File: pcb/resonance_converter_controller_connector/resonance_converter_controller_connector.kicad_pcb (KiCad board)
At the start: 4 copper layers, 66.8 x 100 mm, 83 parts, among them J1 Conn_01x02, J10 Conn_01x04, J11 Conn_01x04, J12 Conn_01x02, J13 Conn_01x06, J14 Conn_02x05_Odd_Even, J15 Conn_01x02, J16 Conn_01x02, J17 Conn_01x02, J18 Conn_01x08, J19 Conn_01x02, J2 Conn_01x02, J20 Conn_01x02, J3 Conn_01x02, J4 Conn_01x04, J5 Conn_01x02, J6 FX18-120S-0.8SH, J7 Conn_01x04, J8 Conn_01x04, J9 Conn_01x04, Q1 Q_NMOS_GDS, Q2 Q_NMOS_GDS, Q3 Q_NMOS_GDS, Q4 Q_NMOS_GDS, Q5 Q_NPN_BEC, SW1 SW_DIP_x01, U1 PCF8574RGTR, U2 MIC29302AWU, U23 TPS2412D, U3 74LVC1G04, U4 TPS2412D, U5 TPS2412D, U6 TPS2412D, U7 TL431D, U8 AT24CS01-SSHM, U9 UA78M33QDCYRQ1

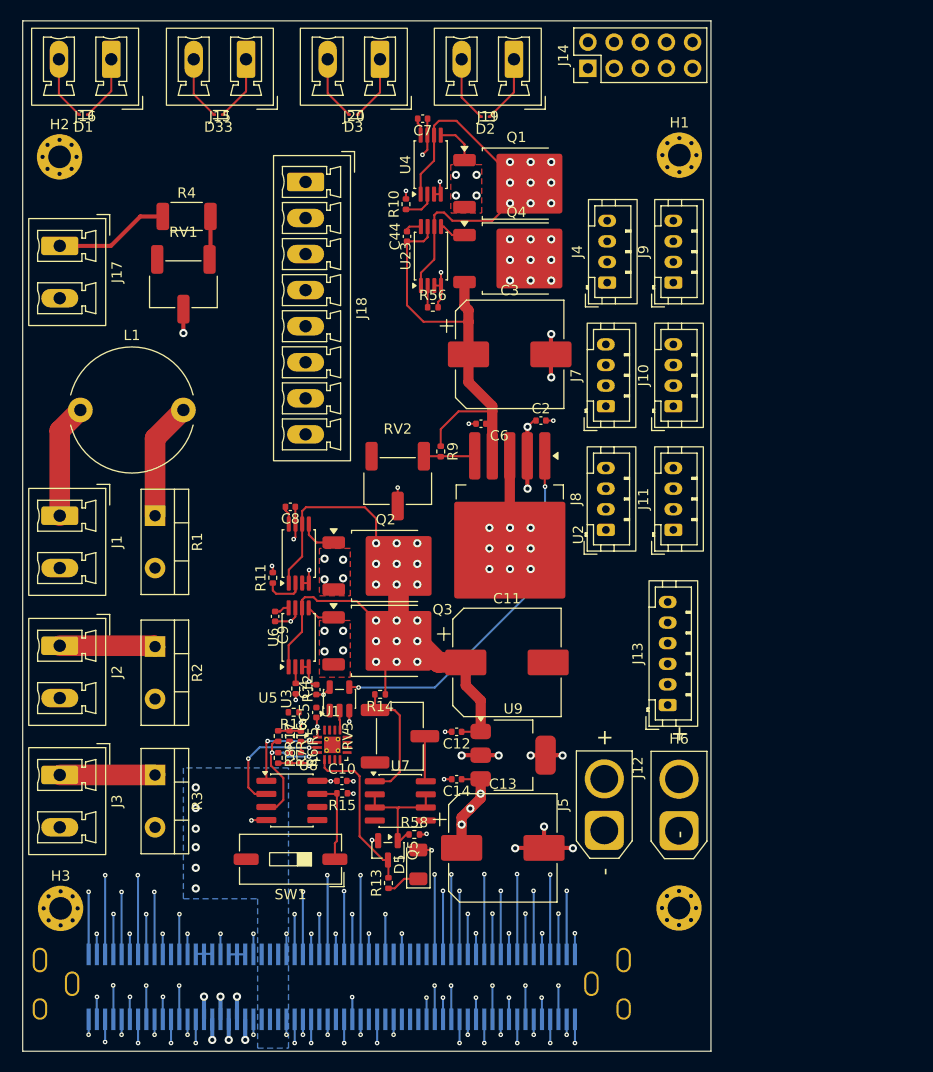
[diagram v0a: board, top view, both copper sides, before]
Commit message: connctor board routed
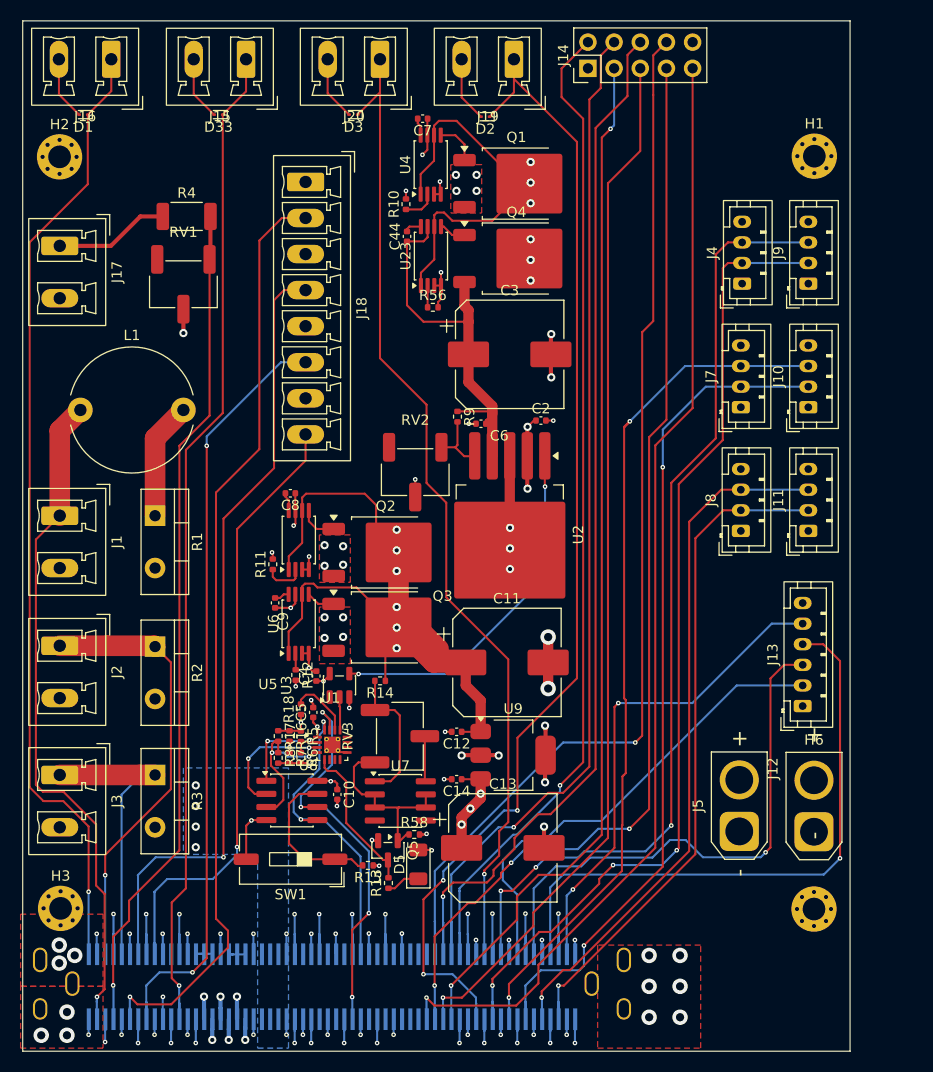
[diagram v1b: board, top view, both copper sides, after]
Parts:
- moved H1 13.1 mm to (192.0, 63.4)
- moved J5 13.1 mm to (184.8, 129.0)
- moved H6 13.1 mm to (192.0, 136.5)
- moved J12 13.1 mm to (192.0, 129.0)
- moved J13 13.1 mm to (190.9, 116.8)
- moved J10 13.1 mm to (191.4, 87.8)
- moved J11 13.1 mm to (191.4, 99.8)
- moved J4 13.1 mm to (185.0, 75.8)
- moved J7 13.1 mm to (184.9, 87.8)
- moved J8 13.1 mm to (184.9, 99.8)
- moved J9 13.1 mm to (191.4, 75.8)
- moved R15 7.43 mm to (148.7, 132.3)
- moved R9 3.75 mm to (157.4, 88.7)
- moved RV2 1.91 mm to (153.3, 94.1)
- moved C10 1.39 mm to (145.7, 125.4), turned to -90 degrees
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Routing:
- net GPIO3: track 2.05 -> 109.2 mm
- net GPIO2: track 3.23 -> 107.9 mm, vias 1 -> 3
- net AUX_PWM_CH1: track 8.60 -> 112.6 mm, vias 1 -> 3
- net GPIO1: track 2.05 -> 102.3 mm
- net GPIO4: track 7.72 -> 105.1 mm
- net GPIO0: track 3.23 -> 100.2 mm, vias 1 -> 2
- net GPIO5: track 6.11 -> 102.1 mm
- net OUT_SYNC_1-: track 3.22 -> 95.7 mm, vias 1 -> 3
- net GPIO6: track 7.71 -> 100.0 mm
- net GPIO7: track 6.11 -> 97.7 mm
- net ISENSE_1: track 2.14 -> 91.6 mm
- net DAC_OUT: track 9.53 -> 98.0 mm
- net OUT_SYNC_1+: track 6.11 -> 92.0 mm, vias 1 -> 3
- net OUT_SYNC_2+: track 2.05 -> 85.7 mm, vias 1 -> 2
- net AUX_PWM_CH2: track 14.0 -> 96.1 mm
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- added copper zone on In4.Cu, net GND
- removed copper zone on In2.Cu, net GND
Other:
- board size 66.8 x 100 mm -> 80.3 x 100 mm
- copper layers 4 -> 6

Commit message: Fix silkscreen
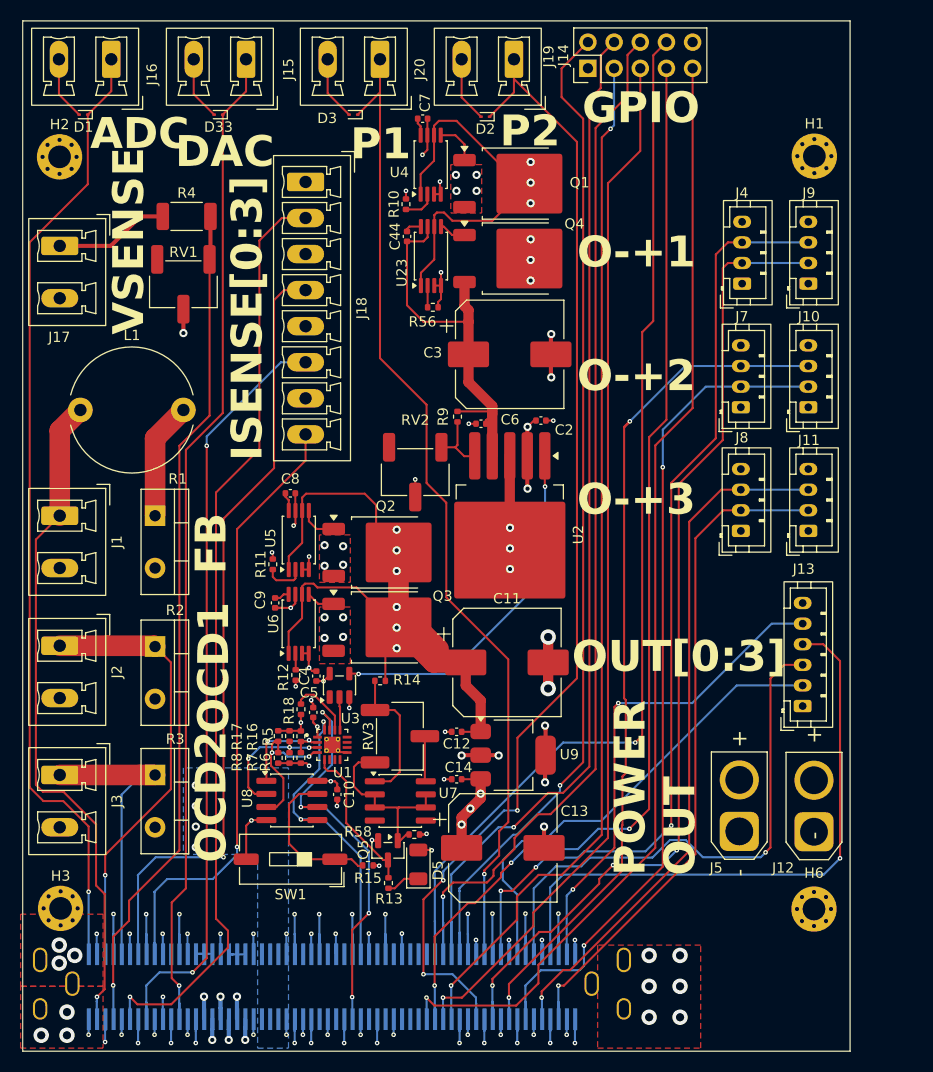
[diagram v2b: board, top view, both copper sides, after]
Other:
- board text added: "ADC"
- board text added: "DAC"
- board text added: "FB"
- board text added: "GPIO"
- board text added: "ISENSE[0:3]"
- board text added: "O-+1"
- board text added: "O-+2"
- board text added: "O-+3"
- board text added: "OCD1"
- board text added: "OCD2"
- board text added: "OUT[0:3]"
- board text added: "P1"
- board text added: "P2"
- board text added: "POWER OUT"
- board text added: "VSENSE"

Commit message: Reduce copper layers as it fits on 4
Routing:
- added copper zone on In2.Cu, net GND
- removed copper zone on In4.Cu, net GND
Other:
- copper layers 6 -> 4
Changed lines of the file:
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@@
 	(generator_version "10.0")
 	(general
-		(thickness 1.6)
+		(thickness 2.836)
 		(legacy_teardrops no)
 	)
@@
 		(0 "F.Cu" signal)
 		(4 "In1.Cu" power "VCC")
-		(6 "In2.Cu" signal "SIG2")
-		(8 "In3.Cu" signal "SIG")
-		(10 "In4.Cu" power "GND")
+		(6 "In2.Cu" signal "GND")
 		(2 "B.Cu" signal)
 		(9 "F.Adhes" user "F.Adhesive")
@@
 			(layer "dielectric 2"
 				(type "core")
-				(thickness 0.535)
+				(thickness 2.476)
 				(material "FR4")
 				(epsilon_r 4.5)
@@
 				(loss_tangent 0.02)
 			)
-			(layer "In3.Cu"
-				(type "copper")
-				(thickness 0.035)
-			)
-			(layer "dielectric 4"
-				(type "core")
-				(thickness 0.535)
-				(material "FR4")
-				(epsilon_r 4.5)
-				(loss_tangent 0.02)
-			)
-			(layer "In4.Cu"
-				(type "copper")
-				(thickness 0.035)
-			)
-			(layer "dielectric 5"
-				(type "prepreg")
-				(thickness 0.1)
-				(material "FR4")
-				(epsilon_r 4.5)
-				(loss_tangent 0.02)
-			)
 			(layer "B.Cu"
 				(type "copper")
@@
 			(remove_unused_layers yes)
 			(keep_end_layers yes)
-			(zone_layer_connections)
+			(zone_layer_connections "In1.Cu")
 			(net "VSYS")
 			(pinfunction "MF_A1")
@@
 	(zone
 		(net "GND")
-		(layer "In4.Cu")
+		(layer "In2.Cu")
 		(hatch edge 0.5)
 		(connect_pads

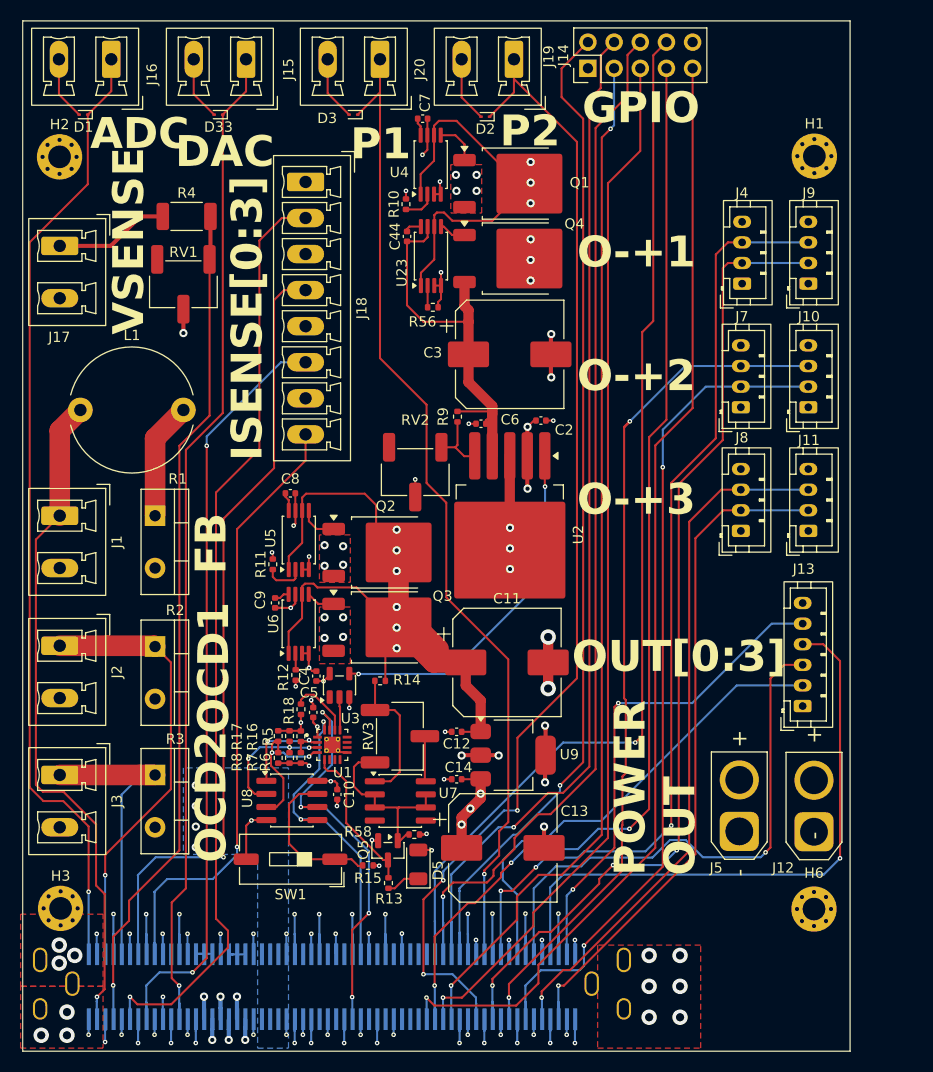
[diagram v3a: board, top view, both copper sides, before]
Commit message: Add 3rd row of output connectors
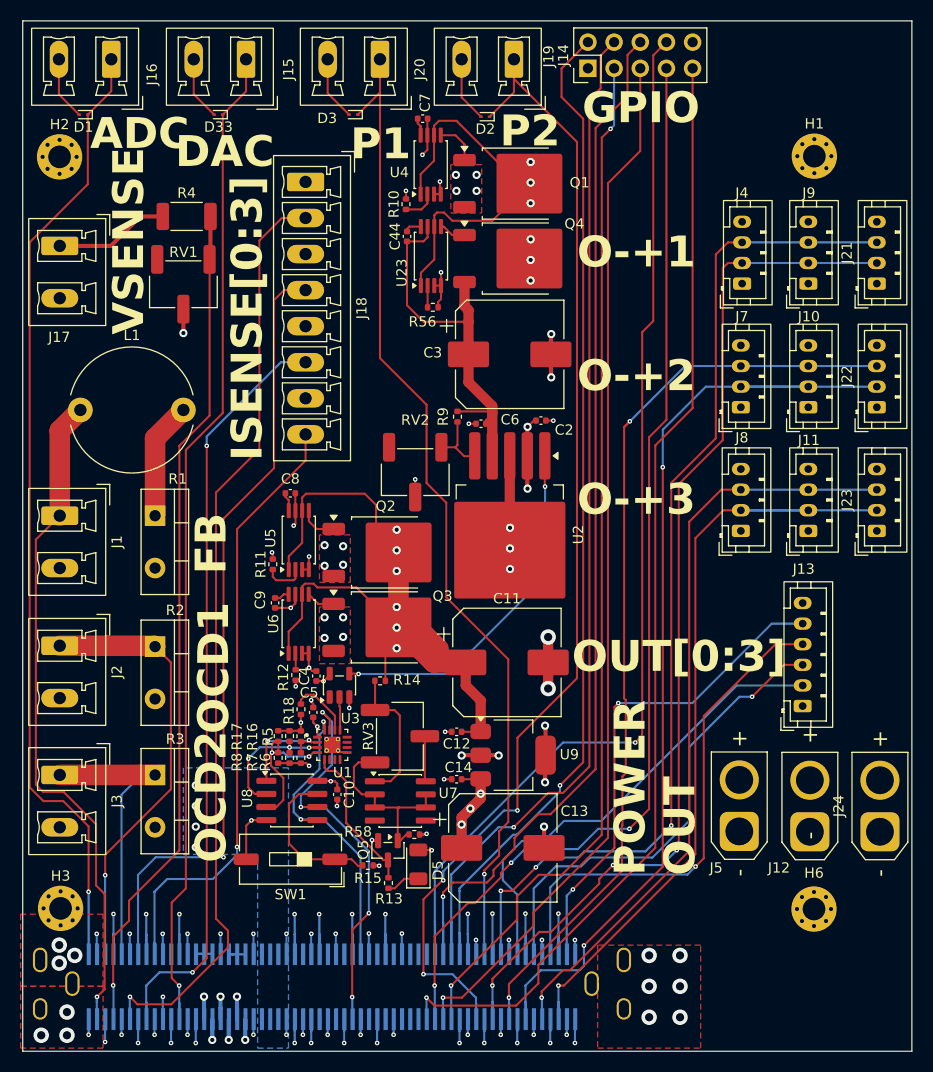
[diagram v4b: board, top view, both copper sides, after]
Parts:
- added J21: Conn_01x04, Connector_JST:JST_PH_B4B-PH-K_1x04_P2.00mm_Vertical, F.Cu at (198.1, 75.8)
- added J22: Conn_01x04, Connector_JST:JST_PH_B4B-PH-K_1x04_P2.00mm_Vertical, F.Cu at (198.1, 87.8)
- added J23: Conn_01x04, Connector_JST:JST_PH_B4B-PH-K_1x04_P2.00mm_Vertical, F.Cu at (198.1, 99.8)
- added J24: Conn_01x02, Connector_AMASS:AMASS_XT30U-M_1x02_P5.0mm_Vertical, F.Cu at (198.4, 129.0)
- moved J12 0.40 mm to (191.6, 129.0)
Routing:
- net OUT_SYNC_3-: track 66.2 -> 79.4 mm
- net OUT_SYNC_2-: track 82.4 -> 95.6 mm
- net OUT2: track 60.0 -> 49.6 mm
- net OUT3: track 52.5 -> 45.7 mm
- net OUT_SYNC_1-: track 95.7 -> 102.4 mm
- net OUT_SYNC_3+: track 68.5 -> 75.1 mm
- net OUT_SYNC_2+: track 85.7 -> 92.3 mm
- net OUT_SYNC_1+: track 92.0 -> 98.7 mm
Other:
- board size 80.3 x 100 mm -> 86.3 x 100 mm
